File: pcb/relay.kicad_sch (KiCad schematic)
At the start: 11 parts, among them K1 PR24-5V-900-1A, P1 MountingHole_Pad, P2 MountingHole_Pad, P3 MountingHole_Pad, P4 MountingHole_Pad, Q1 MMBT3904, U3 LTV-356T

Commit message: initial checkin
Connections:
- net +5V: no longer U3.4
- new net +3.3V: U3.4
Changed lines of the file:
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@@
+	)
+	(symbol
+		(lib_id "power:+3.3V")
+		(at 83.82 58.42 0)
+		(unit 1)
+		(exclude_from_sim no)
+		(in_bom yes)
+		(on_board yes)
+		(dnp no)
+		(fields_autoplaced yes)
+		(property "Reference" "#PWR018"
+			(at 83.82 62.23 0)
+			(effects
+				(font
+					(size 1.27 1.27)
+				)
+				(hide yes)
+			)
+		)
+		(property "Value" "+3.3V"
+			(at 83.82 53.34 0)
+			(effects
+				(font
+					(size 1.27 1.27)
+				)
+			)
+		)
+		(property "Footprint" ""
+			(at 83.82 58.42 0)
+			(effects
+				(font
+					(size 1.27 1.27)
+				)
+				(hide yes)
+			)
+		)
+		(property "Datasheet" ""
+			(at 83.82 58.42 0)
+			(effects
+				(font
+					(size 1.27 1.27)
+				)
+				(hide yes)
+			)
+		)
+		(property "Description" "Power symbol creates a global label with name \"+3.3V\""
+			(at 83.82 58.42 0)
+			(effects
+				(font
+					(size 1.27 1.27)
+				)
+				(hide yes)
+			)
+		)
+		(pin "1"
+		)
+		(instances
+			(project "relay-module"
+				(path "/445c1fff-2e1a-48b1-a91f-a137832edebf/5a0ae98e-a922-4c0c-a9cd-41ef326d2191"
+					(reference "#PWR018")
+					(unit 1)
+				)
+			)
+		)
 	)
 	(symbol
@@
 					(unit 1)
 				)
-			)
-		)
-	)
-	(symbol
-		(lib_id "power:+5V")
-		(at 83.82 58.42 0)
-		(unit 1)
-		(exclude_from_sim no)
-		(in_bom yes)
-		(on_board yes)
-		(dnp no)
-		(fields_autoplaced yes)
-		(property "Reference" "#PWR03"
-			(at 83.82 62.23 0)
-			(effects
-				(font
-					(size 1.27 1.27)
-				)
-				(hide yes)
-			)
-		)
-		(property "Value" "+5V"
-			(at 83.82 53.34 0)
-			(effects
-				(font
-					(size 1.27 1.27)
-				)
-			)
-		)
-		(property "Footprint" ""
-			(at 83.82 58.42 0)
-			(effects
-				(font
-					(size 1.27 1.27)
-				)
-				(hide yes)
-			)
-		)
-		(property "Datasheet" ""
-			(at 83.82 58.42 0)
-			(effects
-				(font
-					(size 1.27 1.27)
-				)
-				(hide yes)
-			)
-		)
-		(property "Description" "Power symbol creates a global label with name \"+5V\""
-			(at 83.82 58.42 0)
-			(effects
-				(font
-					(size 1.27 1.27)
-				)
-				(hide yes)
-			)
-		)
-		(pin "1"
-		)
-		(instances
-			(project "relay-module"
-				(path "/445c1fff-2e1a-48b1-a91f-a137832edebf/5a0ae98e-a922-4c0c-a9cd-41ef326d2191"
-					(reference "#PWR03")
-					(unit 1)
-				)

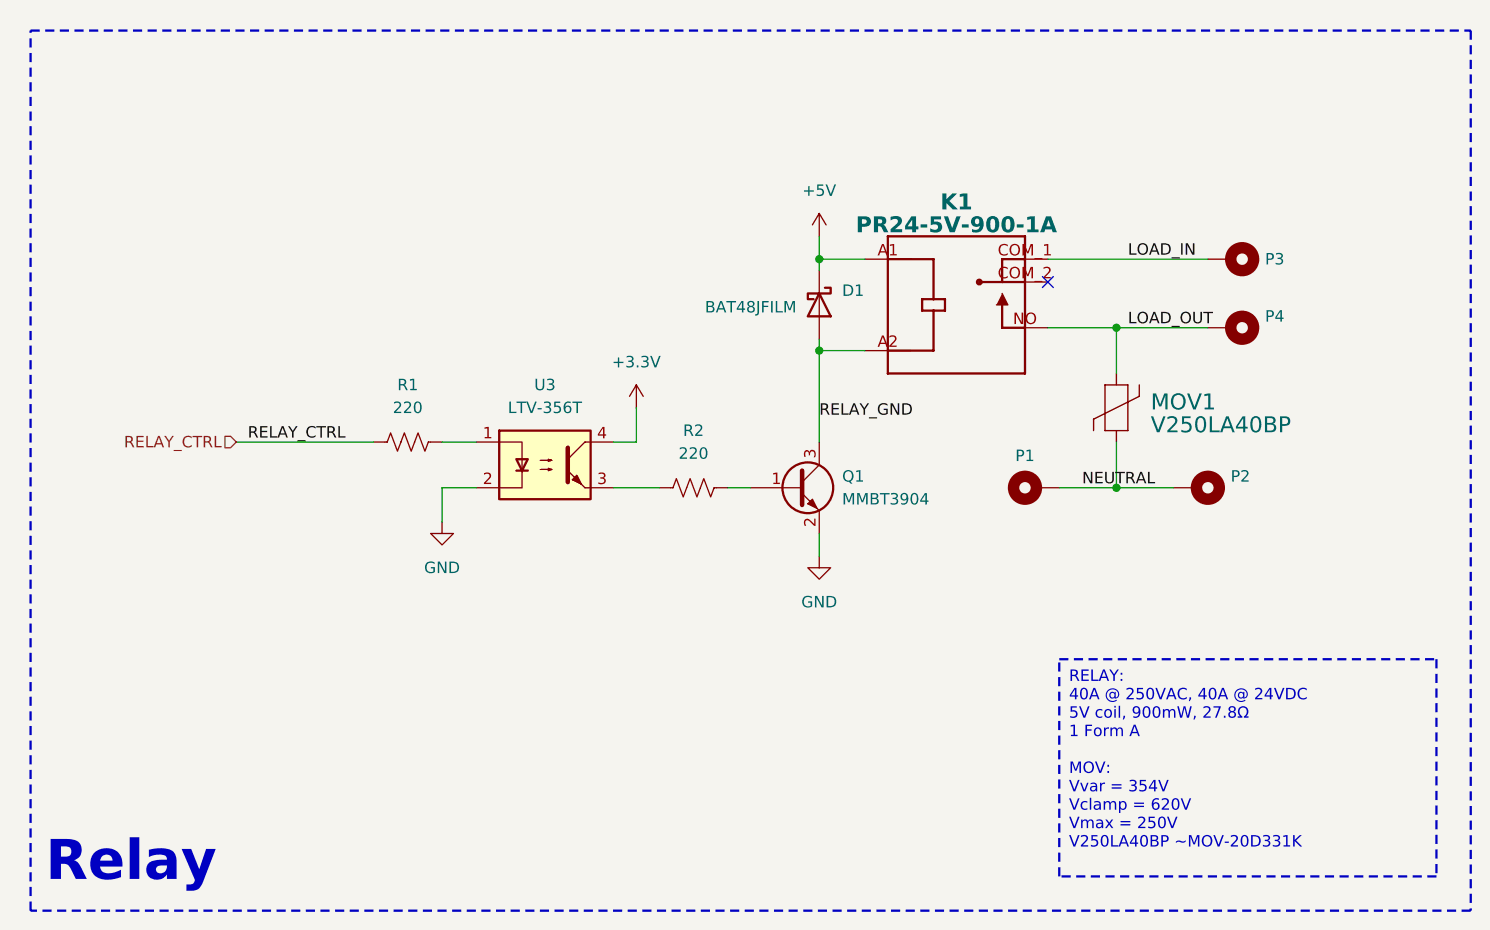
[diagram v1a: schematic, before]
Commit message: Changed to multi-sheet
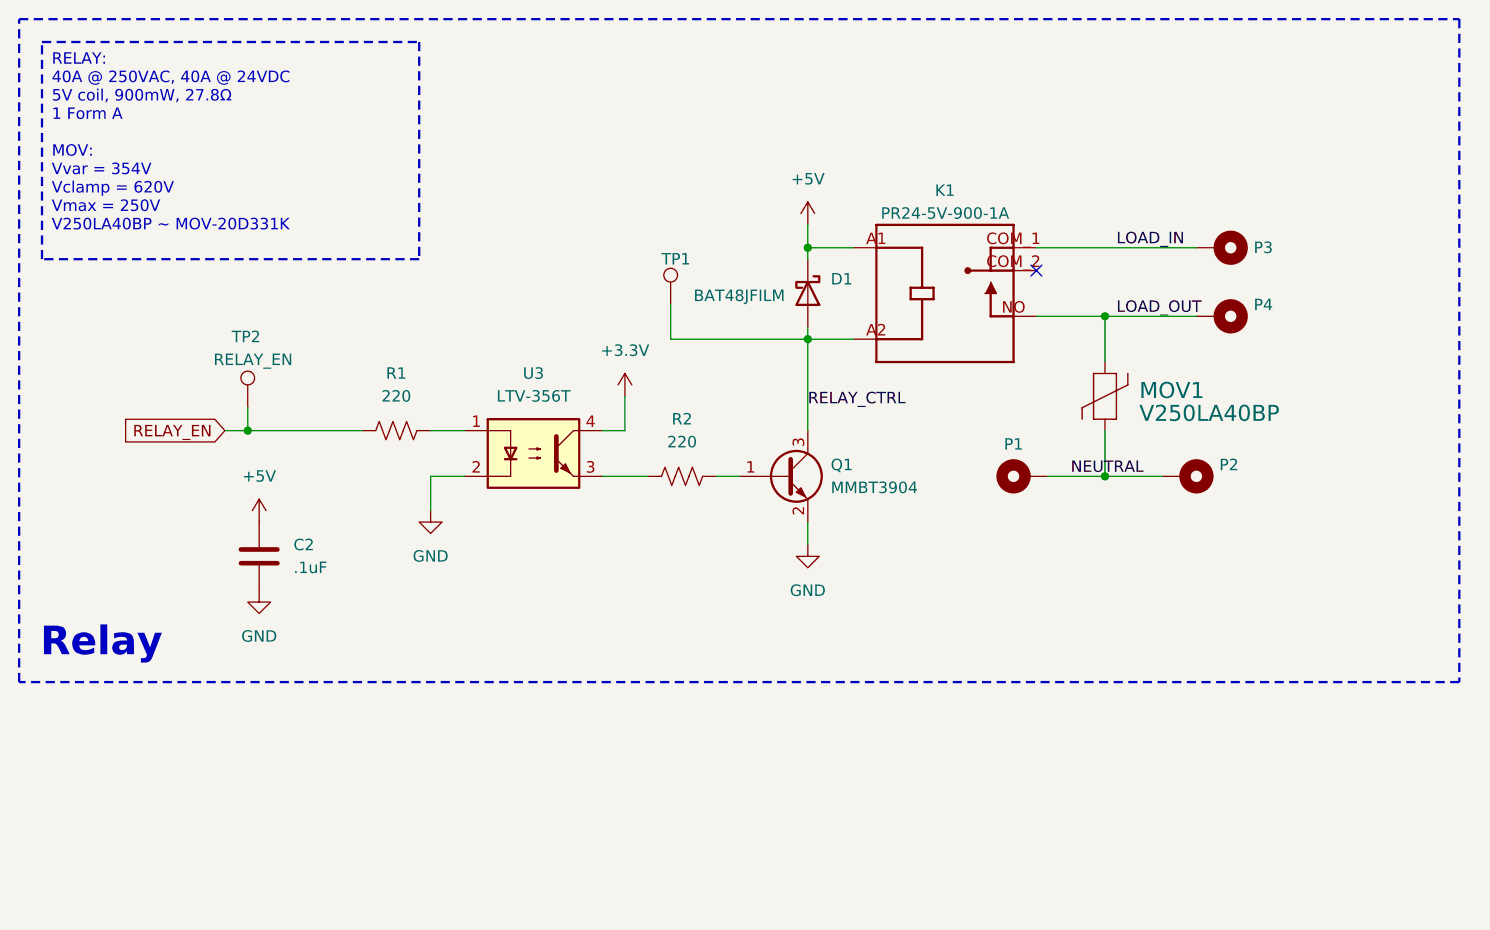
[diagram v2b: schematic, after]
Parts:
- added C2: .1uF, Capacitor_SMD:C_0603_1608Metric, symbol Device:C
- added TP1: RELAY_CTRL, CRGM Mechanical:TestPoint_Pad_D1.0mm, symbol Connector:TestPoint
- added TP2: RELAY_EN, CRGM Mechanical:TestPoint_Pad_D1.0mm, symbol Connector:TestPoint
- D1: LCSC (none) -> C2798199; LCSC_PN C155590 -> (none); MN (none) -> STMicroelectronics; MPN (none) -> BAT48JFILM
- K1: LCSC (none) -> C7029760; LCSC_PN C7029760 -> (none); MN (none) -> Same Sky; MPN (none) -> PR24-5V-900-1A
- MOV1: LCSC (none) -> C1527448; LCSC_PN C1527448 -> (none); MN (none) -> Littlefuse; MPN (none) -> V250LA40BP; now in the parts list
- P1, P2, P3, P4: footprint MountingHole:MountingHole_3.2mm_M3_ISO14580_Pad -> CRGM Mechanical:MountingHole_3.2mm_M3_ISO14580_Pad
- Q1: LCSC (none) -> C909754; LCSC_PN C909754 -> (none); MN (none) -> GOODWORK; MPN (none) -> MMBT3904
- R1, R2: LCSC (none) -> C22962; LCSC_PN C1226 -> (none); MN (none) -> Uni-Royal; MPN (none) -> 0603WAF2200T5E
- U3: LCSC (none) -> C125117; MN (none) -> Lite-On; MPN (none) -> LTV-356T
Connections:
- net RELAY_GND is gone; now on net RELAY_CTRL: D1.2 (A), K1.A2 (COIL2), Q1.3 (C)
- net +5V: now also C2.1
- net GND: now also C2.2
- net RELAY_CTRL: now also TP1.1; no longer R1.1
- new net RELAY_EN: R1.1, TP2.1
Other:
- moved on the sheet: D1, K1, MOV1, P1, P2, P3, P4, R1, R2, U3

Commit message: Updated frame template
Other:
- company: CRG Makes -> (none)
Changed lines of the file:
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@@
 	(title_block
 		(title "Relay Module")
-		(date "2025-03-22")
-		(rev "1.1")
-		(company "CRG Makes")
-		(comment 1 "Aquarius")
 	)
 	(rectangle
